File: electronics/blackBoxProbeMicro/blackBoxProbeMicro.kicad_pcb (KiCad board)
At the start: 4 copper layers, 29 x 29 mm, 60 parts, among them J1 USB-C, J2 JTAG_2X05, J3 JTAG_2X05, J4 DevBoardUartOutput, Q1 Q_NMOS_DUAL, Q2 Q_PMOS_DUAL, U1 MCP1702-MB, U2 USBLC6-2, U3 STM32F103CBT, Y1 8MHz

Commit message: further routing
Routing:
- net /TARGET_PWR_SENSE: track 7.94 -> 22.8 mm, vias 1 -> 2
- net /PROBE_I_RST_SEN: track 6.14 -> 19.0 mm, vias 1 -> 2
- net /MCU_TMS: track 30.8 -> 28.2 mm
- net /TARGET_PWR_EN: track 9.69 -> 11.0 mm

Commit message: further routing
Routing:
- net /TARGET_PWR_EN: track 11.0 -> 20.7 mm, vias 1 -> 2
- net /MCU_TDI: track 31.4 -> 28.8 mm
- net /MCU_TCK: track 33.4 -> 31.0 mm
- net /TARGET_PWR_SENSE: track 22.8 -> 21.0 mm
- net /PROBE_I_RST_SEN: track 19.0 -> 17.2 mm
- net /MCU_TDO: track 32.1 -> 30.6 mm

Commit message: further routing
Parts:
- moved C5 0.72 mm to (155.2, 101.1)
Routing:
- net /USB_V: track 1.10 -> 29.2 mm, vias 0 -> 2
- net /MCU_RST: track 1.70 -> 23.2 mm, vias 1 -> 2
- net /PROBE_I_RST: track 0.00 -> 18.3 mm, vias 0 -> 2
- net /VUSB: track 7.93 -> 25.1 mm, vias 1 -> 2
- net /PROBE_E_RST: track 0.00 -> 15.3 mm, vias 0 -> 1
- net /VSS: track 46.3 -> 49.7 mm, vias 19 -> 20
- net /VDD: track 28.2 -> 29.3 mm
- net /TARGET_PWR_SENSE: track 21.0 -> 21.8 mm
- net /TARGET_PWR_EN: track 20.7 -> 21.5 mm
- net /PROBE_VDD: vias 2 -> 0

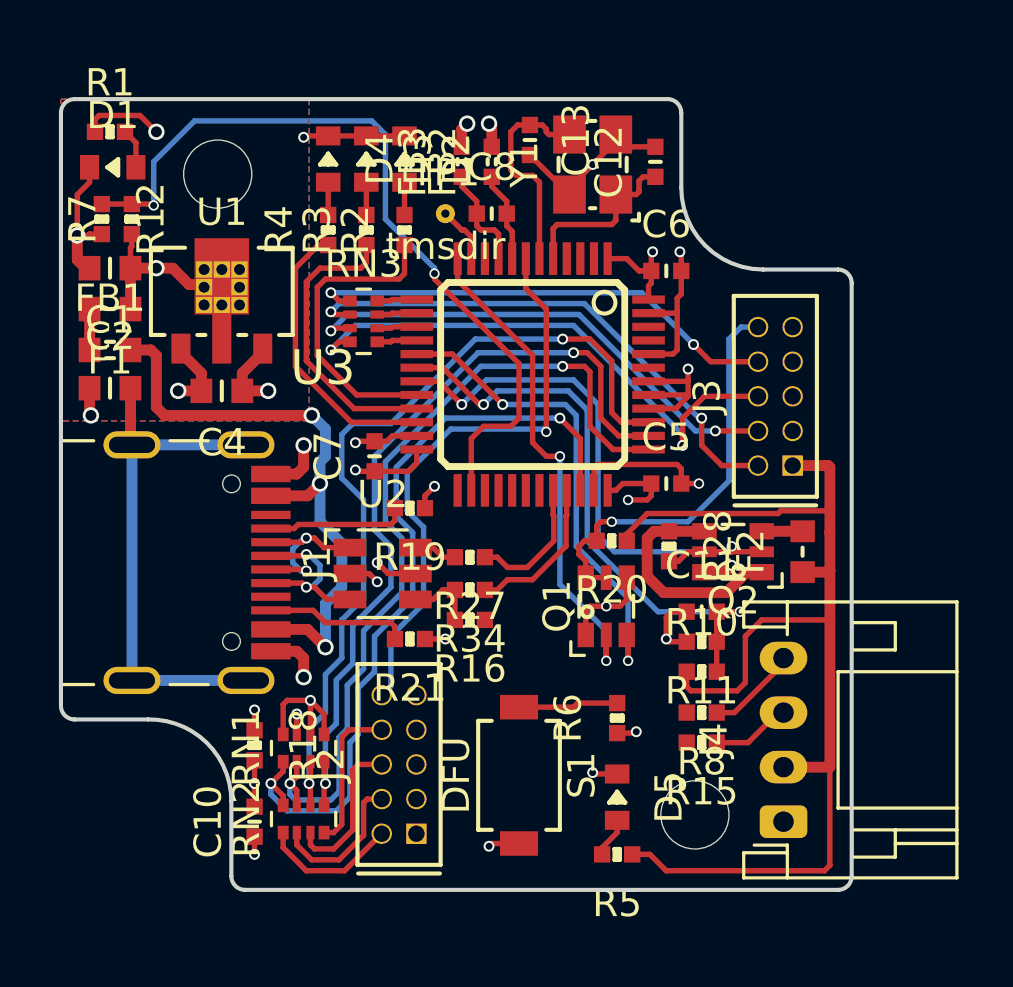
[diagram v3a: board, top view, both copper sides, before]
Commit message: routed everything, time for silk placement
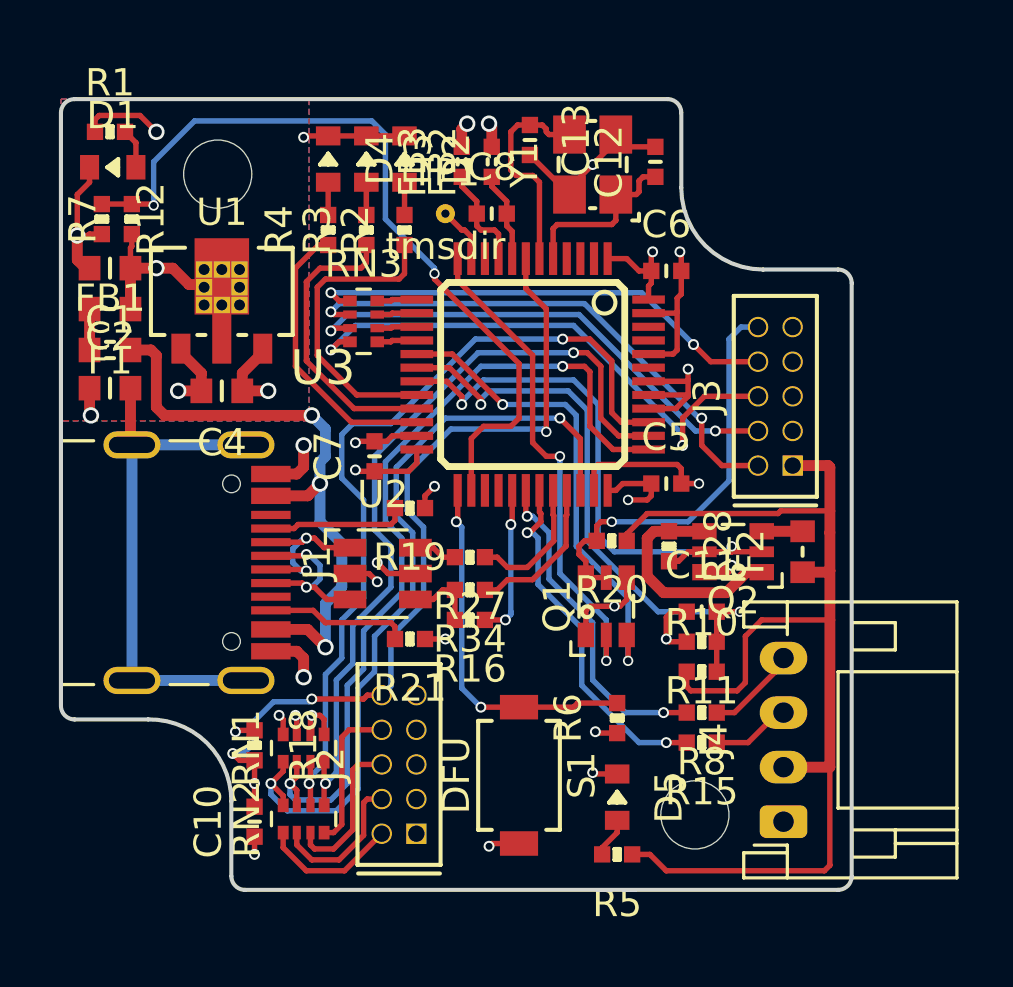
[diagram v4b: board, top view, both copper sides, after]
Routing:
- net /PROBE_I_RX: track 0.00 -> 13.1 mm, vias 0 -> 2
- net /PROBE_I_TX: track 0.00 -> 12.0 mm, vias 0 -> 2
- net /BUTTON: track 3.66 -> 13.4 mm, vias 0 -> 2
- net /MCU_RST: track 23.2 -> 30.9 mm, vias 2 -> 4
- net /USB_PU: track 0.00 -> 5.60 mm, vias 0 -> 2
- net /VDD: track 29.3 -> 27.1 mm, vias 11 -> 12

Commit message: silk optimizations
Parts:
- moved R1 1.53 mm to (135.1, 89.7)
- moved D1 1.10 mm to (135.0, 88.4)
- moved R2 0.30 mm to (145.3, 91.8)
- moved R4 0.30 mm to (143.1, 91.8)
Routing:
- net /VDD: track 27.1 -> 24.8 mm
- net /VSS: track 49.7 -> 50.7 mm, vias 20 -> 21
- net /LED0: track 11.2 -> 10.6 mm
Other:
- board text added: "Power"

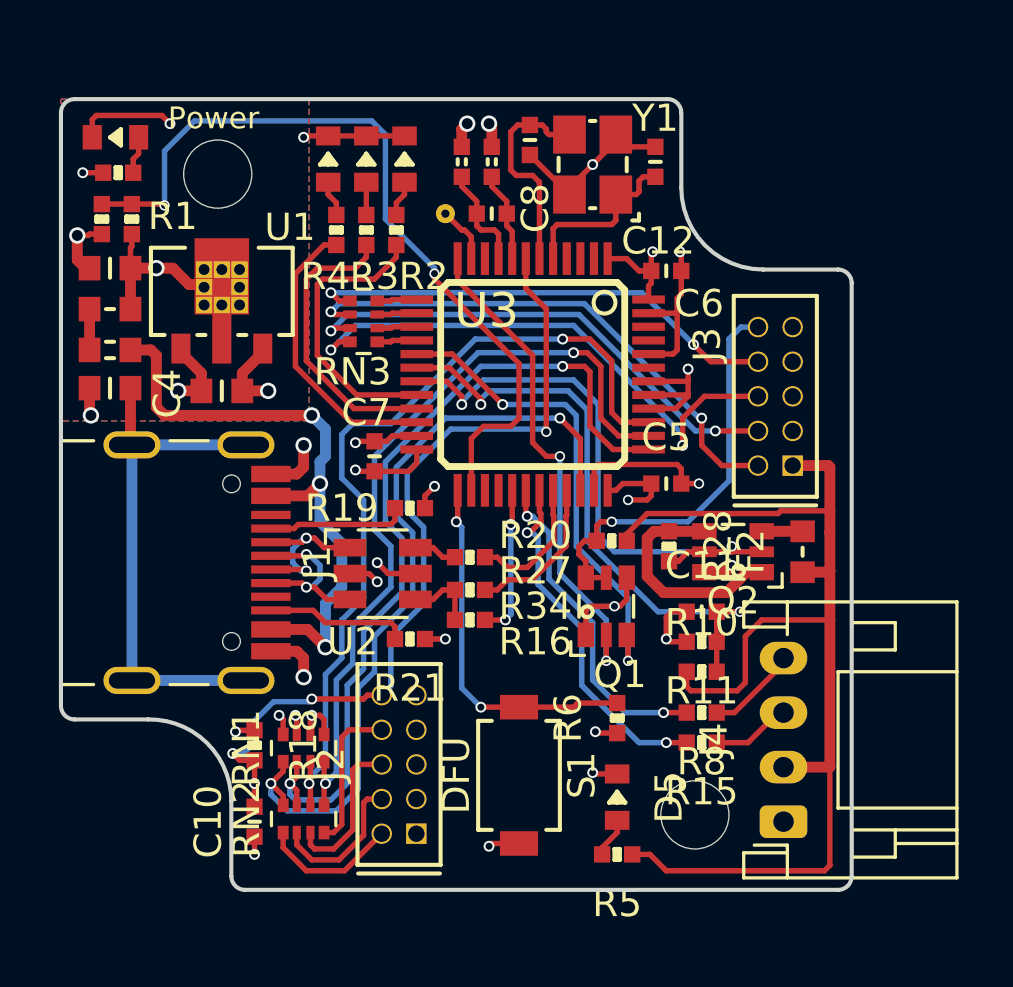
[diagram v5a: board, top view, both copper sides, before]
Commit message: some minor trace optimizations
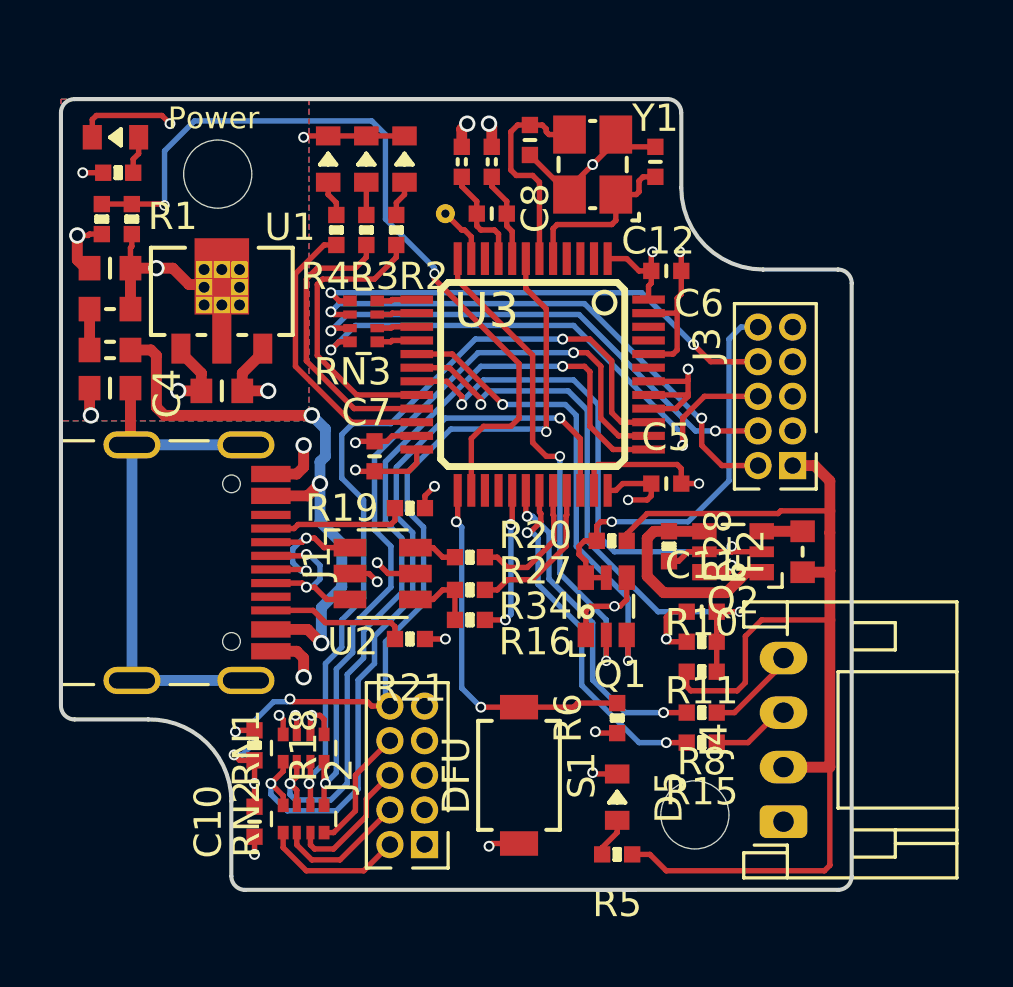
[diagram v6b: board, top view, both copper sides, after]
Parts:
- N2: value V:20210615 -> V:20210620
- moved J2 0.50 mm to (145.7, 111.8)
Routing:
- net Net-(J2-Pad8): track 5.55 -> 4.58 mm
- net Net-(J2-Pad6): track 5.70 -> 4.92 mm
- net /MCU_RST: track 30.9 -> 31.6 mm
- net Net-(J2-Pad4): track 5.42 -> 4.85 mm

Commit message: changed design rules to match 4 layer specs, passing DRC, silk placement
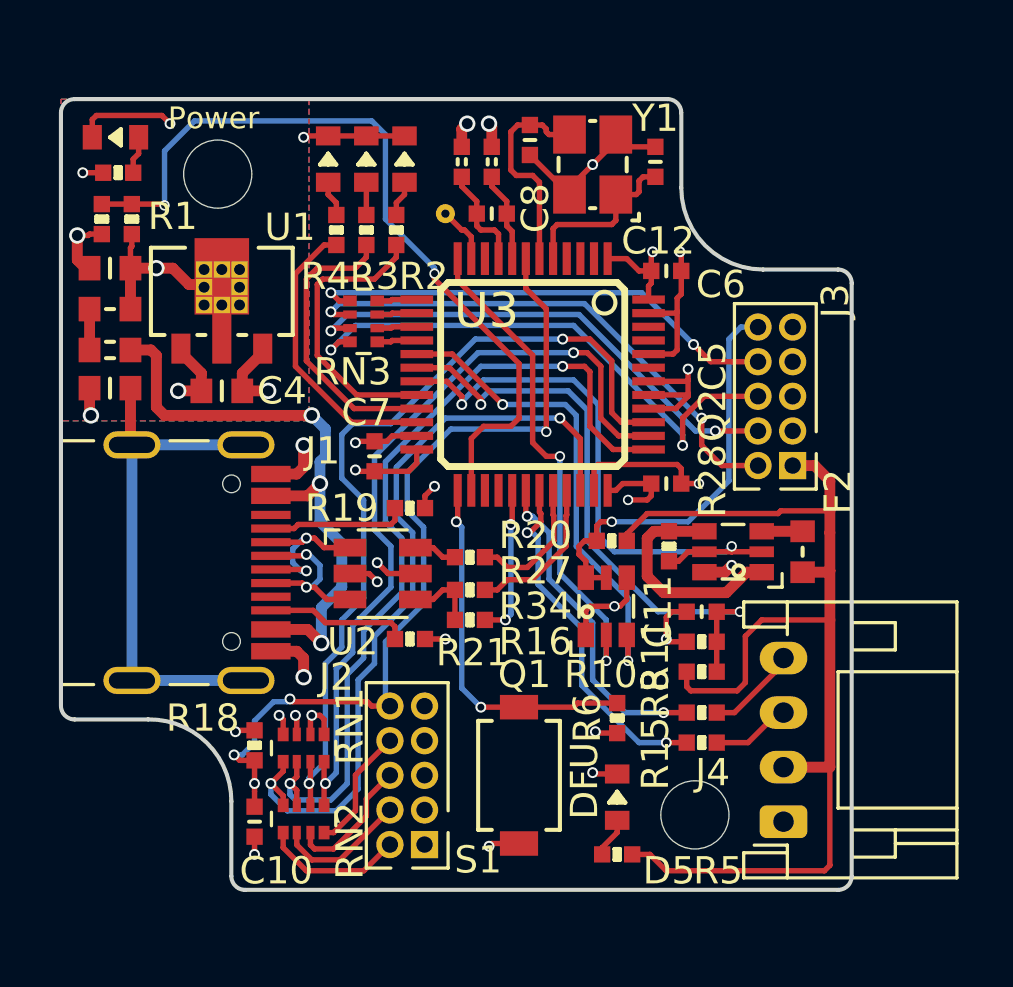
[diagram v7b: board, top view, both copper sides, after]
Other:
- net class Default: clearance 0.1524 -> 0.127; trace_width 0.1524 -> 0.127
- rule trace_clearance: 0.1524 -> 0.127
- rule trace_min: 0.1524 -> 0.127
- rule via_min_size: 0.381 -> 0.254
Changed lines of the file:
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@@
     (user_trace_width 1.5)
     (user_trace_width 2)
-    (trace_clearance 0.1524)
+    (trace_clearance 0.127)
     (zone_clearance 0.3)
     (zone_45_only no)
-    (trace_min 0.1524)
+    (trace_min 0.127)
     (via_size 0.381)
     (via_drill 0.254)
-    (via_min_size 0.381)
+    (via_min_size 0.254)
     (via_min_drill 0.254)
     (user_via 0.4 0.254)
@@
   (net 72 /CC1)
   (net_class Default "This is the default net class."
-    (clearance 0.1524)
-    (trace_width 0.1524)
+    (clearance 0.127)
+    (trace_width 0.127)
     (via_dia 0.381)
     (via_drill 0.254)
@@
     (descr "Header 1.27 2by5 pins")
     (tags "Header 1.27")
-    (fp_text reference J2 (at 0 -2.5 90) (layer F.SilkS)
+    (fp_text reference J2 (at 3.6 -2.6 180) (layer F.SilkS)
       (effects (font (size 1 1) (thickness 0.15)))
     )
@@
     (descr "Header 1.27 2by5 pins")
     (tags "Header 1.27")
-    (fp_text reference J3 (at 1.9 -2.5 90) (layer F.SilkS)
+    (fp_text reference J3 (at 3.5 2.2 90) (layer F.SilkS)
       (effects (font (size 1 1) (thickness 0.15)))
     )
@@
     (tags "resistor 0402")
     (attr smd)
-    (fp_text reference R21 (at 0 -1.8) (layer F.SilkS)
-      (effects (font (size 1 1) (thickness 0.15)))
-    )
-    (fp_text value 5.1K (at 8.3 2.9) (layer F.Fab)
+    (fp_text reference R21 (at -2.3 -0.5) (layer F.SilkS)
+      (effects (font (size 1 1) (thickness 0.15)))
+    )
+    (fp_text value 5.1K (at -2.1 -0.5) (layer F.Fab)
       (effects (font (size 1 1) (thickness 0.15)))
     )
@@
     (tags "resistor array")
     (attr smd)
-    (fp_text reference RN2 (at 0 -2.1 90) (layer F.SilkS)
-      (effects (font (size 1 1) (thickness 0.15)))
-    )
-    (fp_text value 33 (at 0 2.1 90) (layer F.Fab)
+    (fp_text reference RN2 (at -0.8 1.7 90) (layer F.SilkS)
+      (effects (font (size 1 1) (thickness 0.15)))
+    )
+    (fp_text value 33 (at -0.7 1.7 90) (layer F.Fab)
       (effects (font (size 1 1) (thickness 0.15)))
     )
@@
     (tags "resistor array")
     (attr smd)
-    (fp_text reference RN1 (at 0 -2.1 90) (layer F.SilkS)
-      (effects (font (size 1 1) (thickness 0.15)))
-    )
-    (fp_text value 47k (at 0 2.1 90) (layer F.Fab)
+    (fp_text reference RN1 (at 0.8 1.7 90) (layer F.SilkS)
+      (effects (font (size 1 1) (thickness 0.15)))
+    )
+    (fp_text value 47k (at 0.4 1.7 90) (layer F.Fab)
       (effects (font (size 1 1) (thickness 0.15)))
     )
@@
     (tags USB-C)
     (attr smd)
-    (fp_text reference J1 (at 0 -1.7 90) (layer F.SilkS)
-      (effects (font (size 1 1) (thickness 0.15)))
-    )
-    (fp_text value USB-C (at 0 -1.7 90) (layer F.Fab)
+    (fp_text reference J1 (at -4.1 -1.9 180) (layer F.SilkS)
+      (effects (font (size 1 1) (thickness 0.15)))
+    )
+    (fp_text value USB-C (at -4.1 -2.2 180) (layer F.Fab)
       (effects (font (size 1 1) (thickness 0.15)))
     )
@@
     (at 149.8 111.8 270)
     (attr smd)
-    (fp_text reference S1 (at 0 -2.3 90) (layer F.SilkS)
-      (effects (font (size 1 1) (thickness 0.15)))
-    )
-    (fp_text value DFU (at 0 2.3 90) (layer F.SilkS)
+    (fp_text reference S1 (at 3.1 1.5 180) (layer F.SilkS)
+      (effects (font (size 1 1) (thickness 0.15)))
+    )
+    (fp_text value DFU (at 0.2 -2.4 90) (layer F.SilkS)
       (effects (font (size 1 1) (thickness 0.15)))
     )
@@
     (tags "resistor 0402")
     (attr smd)
-    (fp_text reference R15 (at 0 -1.8) (layer F.SilkS)
+    (fp_text reference R15 (at 1.7 -0.4 90) (layer F.SilkS)
       (effects (font (size 1 1) (thickness 0.15)))
     )
@@
     (tags "resistor 0402")
     (attr smd)
-    (fp_text reference R8 (at 0 -1.8) (layer F.SilkS)
+    (fp_text reference R8 (at 1.7 0.7 90) (layer F.SilkS)
       (effects (font (size 1 1) (thickness 0.15)))
     )
@@
     (tags "resistor 0402")
     (attr smd)
-    (fp_text reference R5 (at 0 -1.8) (layer F.SilkS)
-      (effects (font (size 1 1) (thickness 0.15)))
-    )
-    (fp_text value 1K (at 0 1.8) (layer F.Fab)
+    (fp_text reference R5 (at -3.7 -0.6) (layer F.SilkS)
+      (effects (font (size 1 1) (thickness 0.15)))
+    )
+    (fp_text value 1K (at -3.7 -0.6) (layer F.Fab)
       (effects (font (size 1 1) (thickness 0.15)))
     )
@@
     (tags "LED 0603")
     (attr smd)
-    (fp_text reference D5 (at 0 -1.9 90) (layer F.SilkS)
-      (effects (font (size 1 1) (thickness 0.15)))
-    )
-    (fp_text value red (at 0 1.9 90) (layer F.Fab)
+    (fp_text reference D5 (at 2.7 -1.9 180) (layer F.SilkS)
+      (effects (font (size 1 1) (thickness 0.15)))
+    )
+    (fp_text value red (at 2.7 -2 180) (layer F.Fab)
       (effects (font (size 1 1) (thickness 0.15)))
     )
@@
     (tags "resistor 0402")
     (attr smd)
-    (fp_text reference R28 (at 0 -1.8 90) (layer F.SilkS)
+    (fp_text reference R28 (at -2.4 -1.6 90) (layer F.SilkS)
       (effects (font (size 1 1) (thickness 0.15)))
     )
@@
     (tags "resistor 0402")
     (attr smd)
-    (fp_text reference R18 (at 0 -1.8 90) (layer F.SilkS)
-      (effects (font (size 1 1) (thickness 0.15)))
-    )
-    (fp_text value 47K (at 0 1.8 90) (layer F.Fab)
+    (fp_text reference R18 (at -1 1.9 180) (layer F.SilkS)
+      (effects (font (size 1 1) (thickness 0.15)))
+    )
+    (fp_text value 47K (at -1 1.9 180) (layer F.Fab)
       (effects (font (size 1 1) (thickness 0.15)))
     )
@@
     (tags "resistor 0402")
     (attr smd)
-    (fp_text reference R11 (at 0 -1.8) (layer F.SilkS)
+    (fp_text reference R11 (at 1.7 -0.5 90) (layer F.SilkS)
       (effects (font (size 1 1) (thickness 0.15)))
     )
@@
     (tags "resistor 0402")
     (attr smd)
-    (fp_text reference R10 (at 0 -1.8) (layer F.SilkS)
-      (effects (font (size 1 1) (thickness 0.15)))
-    )
-    (fp_text value 4.7K (at 0 1.8) (layer F.Fab)
+    (fp_text reference R10 (at -3.7 0.1) (layer F.SilkS)
+      (effects (font (size 1 1) (thickness 0.15)))
+    )
+    (fp_text value 4.7K (at -3.6 0.1 180) (layer F.Fab)
       (effects (font (size 1 1) (thickness 0.15)))
     )
@@
     (tags "resistor 0402")
     (attr smd)
-    (fp_text reference R6 (at 0 -1.8 90) (layer F.SilkS)
+    (fp_text reference R6 (at 0 -1.1 90) (layer F.SilkS)
       (effects (font (size 1 1) (thickness 0.15)))
     )
@@
     (descr "SOT363 Plastic surface-mounted package; 6 leads SC-88 NXP specification")
     (tags "SOT363-hand SC-88 NXP")
-    (fp_text reference Q2 (at -1.8 0) (layer F.SilkS)
-      (effects (font (size 1 1) (thickness 0.15)))
-    )
-    (fp_text value Q_PMOS_DUAL (at 1.9 0) (layer F.Fab)
+    (fp_text reference Q2 (at 5 -0.75 90) (layer F.SilkS)
+      (effects (font (size 1 1) (thickness 0.15)))
+    )
+    (fp_text value Q_PMOS_DUAL (at 5.2 -0.75 90) (layer F.Fab)
       (effects (font (size 1 1) (thickness 0.15)))
     )
@@
     (descr "SOT363 Plastic surface-mounted package; 6 leads SC-88 NXP specification")
     (tags "SOT363-hand SC-88 NXP")
-    (fp_text reference Q1 (at 0.5 2.5 180) (layer F.SilkS)
+    (fp_text reference Q1 (at -3 2.5) (layer F.SilkS)
       (effects (font (size 1 1) (thickness 0.15)))
     )
@@
     (descr "JST PH series connector, S4B-PH-K (http://www.jst-mfg.com/product/pdf/eng/ePH.pdf), generated with kicad-footprint-generator")
     (tags "connector JST PH top entry")
-    (fp_text reference J4 (at 3 -2.55 90) (layer F.SilkS)
+    (fp_text reference J4 (at 1.8 -2.6 180) (layer F.SilkS)
       (effects (font (size 1 1) (thickness 0.15)))
     )
@@
     (tags "fuse 0603")
     (attr smd)
-    (fp_text reference F2 (at 0 -1.9 90) (layer F.SilkS)
+    (fp_text reference F2 (at 2.2 1.3 270) (layer F.SilkS)
       (effects (font (size 1 1) (thickness 0.15)))
     )
@@
     (tags "capacitor 0402")
     (attr smd)
-    (fp_text reference C11 (at 0 -1.7) (layer F.SilkS)
+    (fp_text reference C11 (at -1.6 0 90) (layer F.SilkS)
       (effects (font (size 1 1) (thickness 0.15)))
     )
@@
     (tags "capacitor 0402")
     (attr smd)
-    (fp_text reference C10 (at 0 -1.7 90) (layer F.SilkS)
-      (effects (font (size 1 1) (thickness 0.15)))
-    )
-    (fp_text value 1u (at 0 1.7 90) (layer F.Fab)
+    (fp_text reference C10 (at -1.8 0.8 180) (layer F.SilkS)
+      (effects (font (size 1 1) (thickness 0.15)))
+    )
+    (fp_text value 1u (at -1.8 0.4 180) (layer F.Fab)
       (effects (font (size 1 1) (thickness 0.15)))
     )
@@
     (tags "capacitor 0402")
     (attr smd)
-    (fp_text reference C6 (at 1.2 1.2) (layer F.SilkS)
+    (fp_text reference C6 (at 2 0.5) (layer F.SilkS)
       (effects (font (size 1 1) (thickness 0.15)))
     )
@@
     (tags "capacitor 0402")
     (attr smd)
-    (fp_text reference C5 (at 0 -1.7) (layer F.SilkS)
-      (effects (font (size 1 1) (thickness 0.15)))
-    )
-    (fp_text value 1u (at 0 1.7) (layer F.Fab)
+    (fp_text reference C5 (at 1.7 -4.3 90) (layer F.SilkS)
+      (effects (font (size 1 1) (thickness 0.15)))
+    )
+    (fp_text value 1u (at 1.7 -4.4 90) (layer F.Fab)
       (effects (font (size 1 1) (thickness 0.15)))
     )
@@
     (tags "capacitor 0603")
     (attr smd)
-    (fp_text reference C4 (at 2 -0.1 90) (layer F.SilkS)
-      (effects (font (size 1 1) (thickness 0.15)))
-    )
-    (fp_text value 10u (at 2 -0.1 90) (layer F.Fab)
-      (effects (font (size 1 1) (thickness 0.15)))
-    )
+    (fp_text reference C4 (at -2.2 0 180) (layer F.SilkS)
+      (effects (font (size 1 1) (thickness 0.15)))
+    )
+    (fp_text value 10u (at -2.7 0 180) (layer F.Fab)
+      (effects (font (size 1 1) (thickness 0.15)))
+    )
